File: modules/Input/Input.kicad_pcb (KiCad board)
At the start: 2 copper layers, 65 x 45 mm, 44 parts, among them J1 Conn_01x04_Male, Q1 MMBT3904, U1 LM1881, U2 LM6172, U3 LM6172, U4 CD4053B

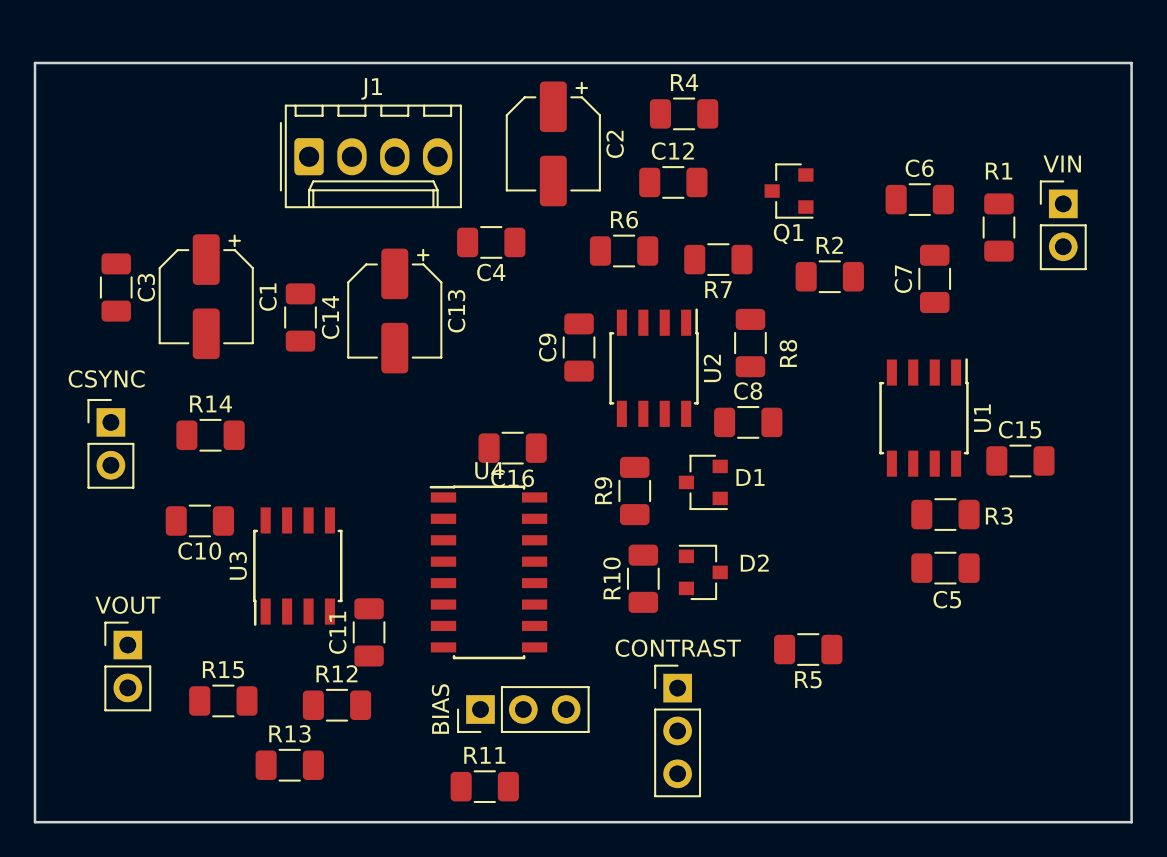
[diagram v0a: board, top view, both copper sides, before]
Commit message: needs silk but otherwise done for now
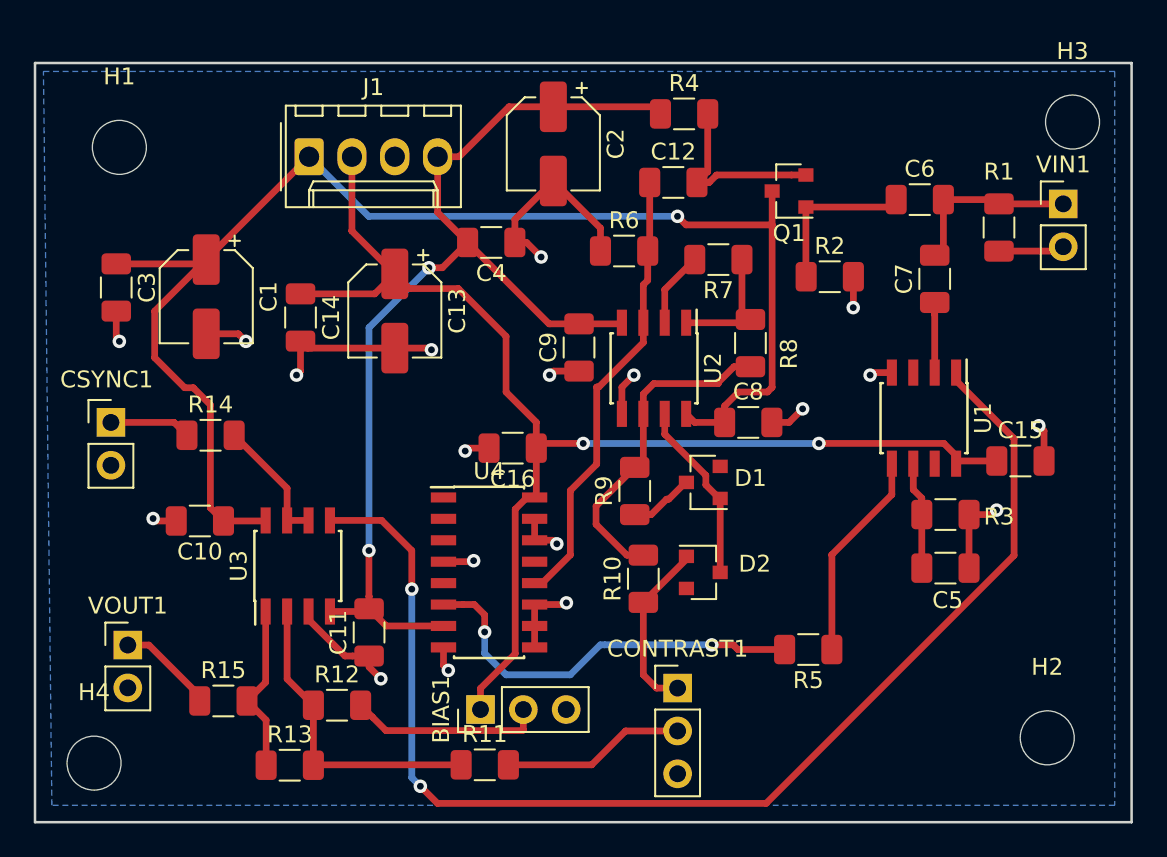
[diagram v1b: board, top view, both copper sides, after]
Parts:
- added H1: MountingHole, MountingHole:MountingHole_3.2mm_M3, F.Cu at (115.0, 65.0)
- added H2: MountingHole, MountingHole:MountingHole_3.2mm_M3, F.Cu at (170.0, 100.0)
- added H3: MountingHole, MountingHole:MountingHole_3.2mm_M3, F.Cu at (171.5, 63.5)
- added H4: MountingHole, MountingHole:MountingHole_3.2mm_M3, F.Cu at (113.5, 101.5)
- moved R11 1.29 mm to (136.7, 101.6)
- renumbered BIAS to BIAS1, CONTRAST to CONTRAST1, CSYNC to CSYNC1, VIN to VIN1, VOUT to VOUT1
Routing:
- net +12V: track 0.00 -> 82.8 mm, vias 0 -> 1
- net +5V: track 0.00 -> 75.0 mm, vias 0 -> 2
- net CSYNC: track 0.00 -> 73.7 mm, vias 0 -> 2
- net GND: track 0.00 -> 67.1 mm, vias 0 -> 19
- net -12V: track 0.00 -> 63.4 mm, vias 0 -> 2
- net Net-(C12-Pad1): track 0.00 -> 27.5 mm
- net Net-(R5-Pad2): track 0.00 -> 24.1 mm, vias 0 -> 2
- net Net-(R10-Pad2): track 0.00 -> 20.0 mm
- net Net-(R11-Pad1): track 0.00 -> 18.5 mm
- net Net-(R5-Pad1): track 0.00 -> 12.5 mm
- net Net-(BIAS1-Pad2): track 0.00 -> 11.5 mm
- net Net-(C12-Pad2): track 0.00 -> 11.0 mm
- net Net-(CONTRAST1-Pad2): track 0.00 -> 10.9 mm
- net Net-(D1-Pad2): track 0.00 -> 10.8 mm
- net Net-(C6-Pad2): track 0.00 -> 10.7 mm
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- added copper zone on B.Cu, net GND
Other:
- net class Default: trace_width 0.25 -> 0.4

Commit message: panels added
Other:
- board text added: "+12"
- board text added: "+5"
- board text added: "-12"
- board text added: "BIAS"
- board text added: "CONTRAST"
- board text added: "CSYNC OUT"
- board text added: "GND"
- board text added: "Input module rev A"
- board text added: "VIDEO INPUT"
- board text added: "VIDEO OUTPUT"
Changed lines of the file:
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@@
   (general
     (thickness 1.6)
-    (drawings 4)
+    (drawings 16)
     (tracks 278)
     (zones 0)
@@
   (layers
     (0 F.Cu signal)
-    (31 B.Cu signal)
+    (31 B.Cu signal hide)
     (32 B.Adhes user)
     (33 F.Adhes user)
@@
     (pad 1 np_thru_hole circle (at 0 0) (size 3.2 3.2) (drill 3.2) (layers *.Cu *.Mask))
   )
+  (gr_text "Input module rev A" (at 160 89.5) (layer B.SilkS)
+    (effects (font (size 1.5 1.5) (thickness 0.3)) (justify mirror))
+  )
+  (gr_text GND (at 132.5 69.5) (layer B.SilkS)
+    (effects (font (size 1.5 1.5) (thickness 0.3)) (justify mirror))
+  )
+  (gr_text +5 (at 128 69.5) (layer B.SilkS)
+    (effects (font (size 1.5 1.5) (thickness 0.3)) (justify mirror))
+  )
+  (gr_text -12 (at 137 62) (layer B.SilkS)
+    (effects (font (size 1.5 1.5) (thickness 0.3)) (justify mirror))
+  )
+  (gr_text +12 (at 124.5 62) (layer B.SilkS)
+    (effects (font (size 1.5 1.5) (thickness 0.3)) (justify mirror))
+  )
+  (gr_text "VIDEO\nOUTPUT" (at 121.5 95.5) (layer B.SilkS)
+    (effects (font (size 1.5 1.5) (thickness 0.3)) (justify mirror))
+  )
+  (gr_text "CSYNC\nOUT" (at 120 82) (layer B.SilkS)
+    (effects (font (size 1.5 1.5) (thickness 0.3)) (justify mirror))
+  )
+  (gr_text "BIAS\n" (at 140 94.5) (layer B.SilkS)
+    (effects (font (size 1.5 1.5) (thickness 0.3)) (justify mirror))
+  )
+  (gr_text CONTRAST (at 156 98) (layer B.SilkS)
+    (effects (font (size 1.5 1.5) (thickness 0.3)) (justify mirror))
+  )
+  (gr_text "VIDEO\nINPUT" (at 165 69.5) (layer B.SilkS)
+    (effects (font (size 1.5 1.5) (thickness 0.3)) (justify mirror))
+  )
+  (dimension 45 (width 0.3) (layer Dwgs.User)
+    (gr_text "45.000 mm" (at 180.1 82.5 270) (layer Dwgs.User)
+      (effects (font (size 1.5 1.5) (thickness 0.3)))
+    )
+    (feature1 (pts (xy 175 105) (xy 178.586421 105)))
+    (feature2 (pts (xy 175 60) (xy 178.586421 60)))
+    (crossbar (pts (xy 178 60) (xy 178 105)))
+    (arrow1a (pts (xy 178 105) (xy 177.413579 103.873496)))
+    (arrow1b (pts (xy 178 105) (xy 178.586421 103.873496)))
+    (arrow2a (pts (xy 178 60) (xy 177.413579 61.126504)))
+    (arrow2b (pts (xy 178 60) (xy 178.586421 61.126504)))
+  )
+  (dimension 65 (width 0.3) (layer Dwgs.User)
+    (gr_text "65.000 mm" (at 142.5 107.1) (layer Dwgs.User)
+      (effects (font (size 1.5 1.5) (thickness 0.3)))
+    )
+    (feature1 (pts (xy 175 105) (xy 175 105.586421)))
+    (feature2 (pts (xy 110 105) (xy 110 105.586421)))
+    (crossbar (pts (xy 110 105) (xy 175 105)))
+    (arrow1a (pts (xy 175 105) (xy 173.873496 105.586421)))
+    (arrow1b (pts (xy 175 105) (xy 173.873496 104.413579)))
+    (arrow2a (pts (xy 110 105) (xy 111.126504 105.586421)))
+    (arrow2b (pts (xy 110 105) (xy 111.126504 104.413579)))
+  )
   (gr_line (start 110 105) (end 110 60) (layer Edge.Cuts) (width 0.15))
